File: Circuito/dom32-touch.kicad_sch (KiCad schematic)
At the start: 41 parts, among them J1 Poste X 5, J2 POWER 5v, J3 CF4240FH0R0-05-NH, J4 DEBUG & Buzzer, J5 MEM2067-02-180-00-A, Q1 BC548, SW1 TactSwitch, U1 ZLDO1117QG33TADICT-ND, U2 PIC32MM0256GPM028-I-SS, U3 1965-ESP-WROOM-02D-N4CT-ND

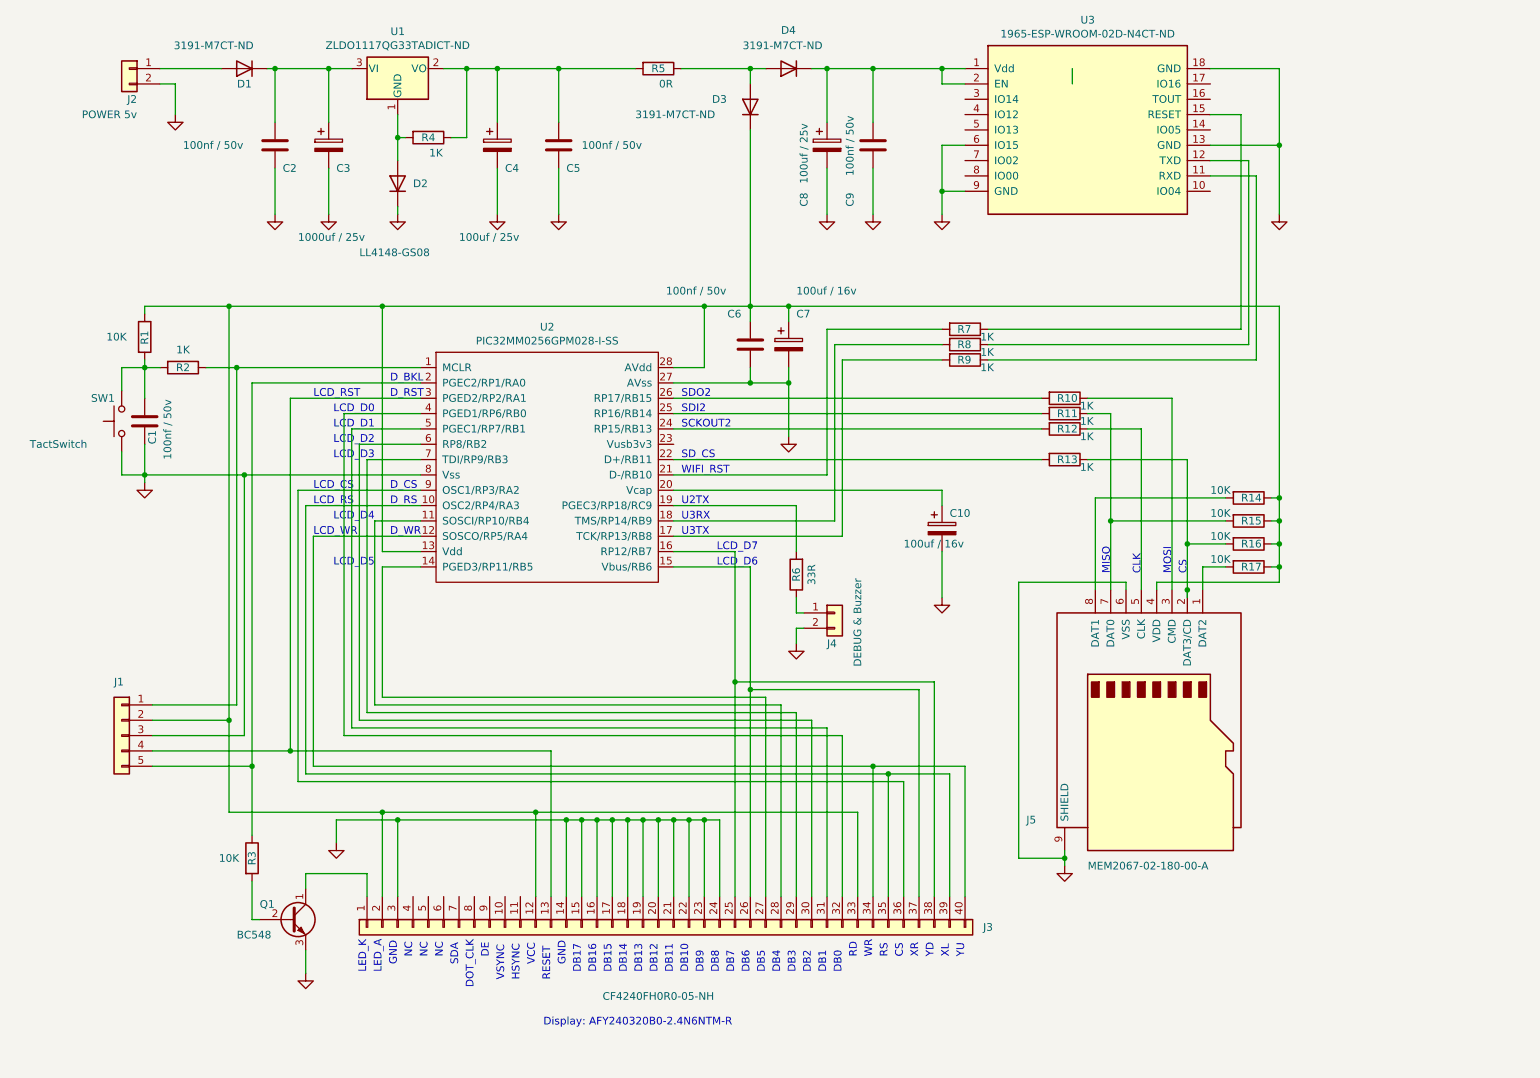
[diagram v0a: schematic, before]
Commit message: Adaptacion display de Orieny Display
Adaptacion display de Orieny Display
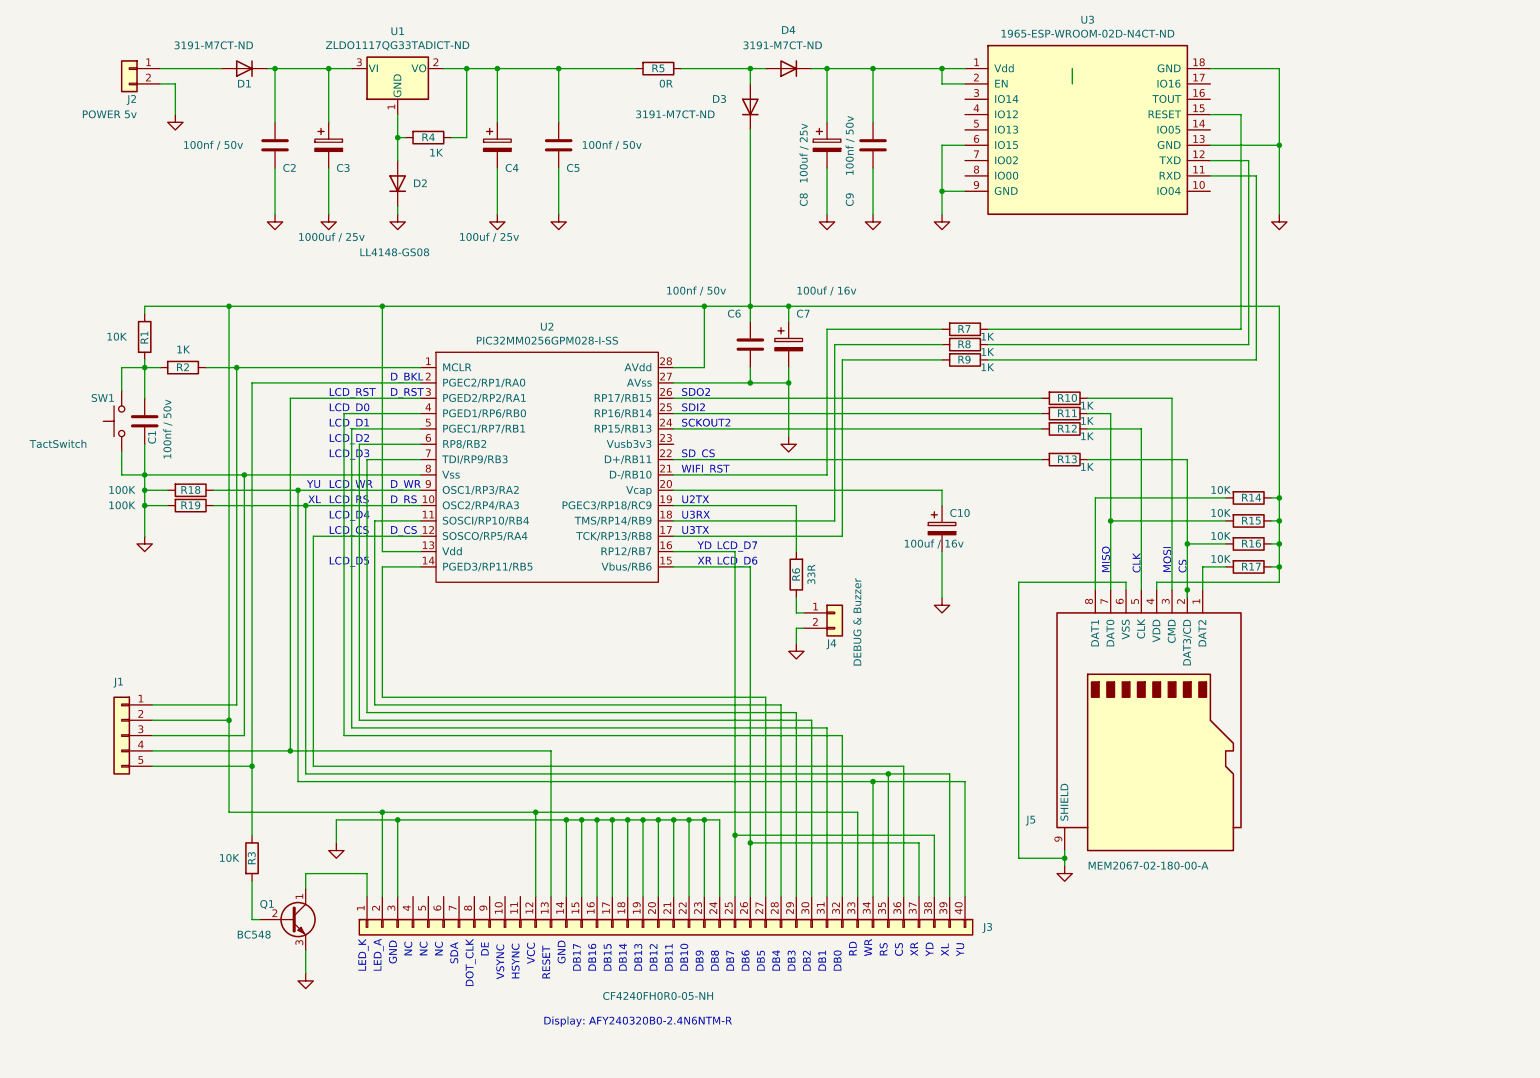
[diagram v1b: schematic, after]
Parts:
- added R18, R19: 100K, Resistor_SMD:R_0805_2012Metric_Pad1.20x1.40mm_HandSolder, symbol Device:R
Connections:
- net GND: now also R18.2, R19.2
- net at J3.35 (Pin_35), J3.39 (Pin_39), U2.10 (OSC2/RP4/RA3): now also R19.1
- net at J3.34 (Pin_34), J3.40 (Pin_40): now also U2.9 (OSC1/RP3/RA2), R18.1; no longer U2.12 (SOSCO/RP5/RA4)
- net at J3.36 (Pin_36): now also U2.12 (SOSCO/RP5/RA4); no longer U2.9 (OSC1/RP3/RA2)

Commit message: Inicio Placa
Inicio Placa
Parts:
- added C2: 100nf / 50v, Capacitor_SMD:C_0805_2012Metric_Pad1.18x1.45mm_HandSolder, symbol Device:C
- J1: Etiqueta (none) -> ICMP
- J2: value POWER 5v -> 277-1667-ND; Etiqueta (none) -> POWER 9v a 12v
- SW1: Etiqueta (none) -> Reset
- renumbered C9 to C10, C10 to C11, C2 to C3, C3 to C4, C4 to C5, C5 to C6, C6 to C7, C7 to C8, C8 to C9, R8 to R10, R9 to R11, R10 to R12, R11 to R13, R12 to R14, R13 to R15, R14 to R16, R15 to R17, R16 to R18, R17 to R19, R18 to R3, R19 to R4, R3 to R5, R4 to R6, R5 to R7, R6 to R8, R7 to R9
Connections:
- net GND: now also J3.10 (Pin_10), J3.11 (Pin_11), J3.7 (Pin_7), J3.8 (Pin_8), J3.9 (Pin_9), C2.1
- net at C7.1, C8.1, D3.1 (K)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: now also C2.2
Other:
- note added: "Dom32-Touch"

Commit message: Circuito Impreso
Circuito Impreso
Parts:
- added D10, D11, D12, D7, D8, D9: Cortesia, Diode_SMD:D_0805_2012Metric_Pad1.15x1.40mm_HandSolder, symbol Device:LED
- added D5: Power Ok, Diode_SMD:D_0805_2012Metric_Pad1.15x1.40mm_HandSolder, symbol Device:LED
- added D6: Error, Diode_SMD:D_0805_2012Metric_Pad1.15x1.40mm_HandSolder, symbol Device:LED
- added R20, R21, R22: 1K, Resistor_SMD:R_0805_2012Metric_Pad1.20x1.40mm_HandSolder, symbol Device:R
- C11, C8: value 100uf / 16v -> 100uf / 25v; footprint Capacitor_THT:CP_Radial_D6.3mm_P2.50mm -> Capacitor_SMD:CP_Elec_6.3x7.7
- C4: footprint Capacitor_THT:CP_Radial_D8.0mm_P5.00mm -> Capacitor_SMD:CP_Elec_6.3x7.7
- C5, C9: footprint Capacitor_THT:CP_Radial_D6.3mm_P2.50mm -> Capacitor_SMD:CP_Elec_6.3x7.7
- Q1: footprint Package_TO_SOT_THT:TO-92_Inline -> Package_TO_SOT_SMD:SOT-23
- SW1: footprint Button_Switch_THT:SW_PUSH_6mm_H5mm -> Button_Switch_SMD:SW_Push_1P1T_NO_6x6mm_H9.5mm
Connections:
- net GND: now also D5.1 (K), D6.1 (K)
- net at C3.1, C4.1, D1.1 (K)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: now also R22.1
- net at J3.1 (Pin_1), Q1.1 (C): now also D12.1 (K), D8.1 (K)
- net at C5.1, C6.1, R6.1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: now also R20.1
- net at R8.2, U2.19 (PGEC3/RP18/RC9): now also R21.2
- new net: D10.1 (K), D11.2 (A)
- new net: D10.2 (A), D9.2 (A), R22.2
- new net: D11.1 (K), D12.2 (A)
- new net: D7.1 (K), D8.2 (A)
- new net: D6.2 (A), R21.1
- new net: D5.2 (A), R20.2
- new net: D7.2 (A), D9.1 (K)
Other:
- moved on the sheet: J4, R8

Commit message: Fabricacion
Fabricacion
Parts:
- C4: value 1000uf / 25v -> 100uf / 25v
- D10, D11, D12, D7, D8, D9: value Cortesia -> Led SMD Azul
- D5: value Power Ok -> Led SMD Verde
- D6: value Error -> Led SMD Rojo
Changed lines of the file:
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@@
       (effects (font (size 1.27 1.27)))
     )
-    (property "Value" "Cortesia" (at 29.21 190.5 0)
+    (property "Value" "Led SMD Azul" (at 29.21 190.5 0)
       (effects (font (size 1.27 1.27)) hide)
     )
@@
       (effects (font (size 1.27 1.27)))
     )
-    (property "Value" "Cortesia" (at 46.99 190.5 0)
+    (property "Value" "Led SMD Azul" (at 46.99 190.5 0)
       (effects (font (size 1.27 1.27)) hide)
     )
@@
       (effects (font (size 1.27 1.27)))
     )
-    (property "Value" "Cortesia" (at 46.99 195.58 0)
+    (property "Value" "Led SMD Azul" (at 46.99 195.58 0)
       (effects (font (size 1.27 1.27)) hide)
     )
@@
       (effects (font (size 1.27 1.27)))
     )
-    (property "Value" "Cortesia" (at 29.21 195.58 0)
+    (property "Value" "Led SMD Azul" (at 29.21 195.58 0)
       (effects (font (size 1.27 1.27)) hide)
     )
@@
       (effects (font (size 1.27 1.27)))
     )
-    (property "Value" "Error" (at 161.29 116.84 90)
+    (property "Value" "Led SMD Rojo" (at 161.29 116.84 90)
       (effects (font (size 1.27 1.27)))
     )
@@
       (effects (font (size 1.27 1.27)))
     )
-    (property "Value" "Power Ok" (at 119.38 46.99 90)
+    (property "Value" "Led SMD Verde" (at 119.38 46.99 90)
       (effects (font (size 1.27 1.27)))
     )
@@
       (effects (font (size 1.27 1.27)) (justify left))
     )
-    (property "Value" "1000uf / 25v" (at 60.96 57.15 0)
+    (property "Value" "100uf / 25v" (at 60.96 57.15 0)
       (effects (font (size 1.27 1.27)) (justify left))
     )
@@
       (effects (font (size 1.27 1.27)))
     )
-    (property "Value" "Cortesia" (at 38.1 190.5 0)
+    (property "Value" "Led SMD Azul" (at 38.1 190.5 0)
       (effects (font (size 1.27 1.27)) hide)
     )
@@
       (effects (font (size 1.27 1.27)))
     )
-    (property "Value" "Cortesia" (at 38.1 195.58 0)
-      (effects (font (size 1.27 1.27)) hide)
-    )
+    (property "Value" "Led SMD Azul" (at 38.1 195.58 0)
+      (effects (font (size 1.27 1.27)) hide)
+    )
